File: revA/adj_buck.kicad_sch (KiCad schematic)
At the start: 31 parts, among them U26 LTC3600, U29 DAC121S101Q, U32 AD5270BRM

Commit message: exported init pdf
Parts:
- renumbered TP1 to TP3, TP2 to TP4
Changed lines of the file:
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@@
   (symbol (lib_id "Connector:TestPoint") (at 337.82 161.29 0) (unit 1)
     (in_bom yes) (on_board yes) (dnp no)
-    (property "Reference" "TP1" (at 340.36 157.353 0)
+    (property "Reference" "TP3" (at 340.36 157.353 0)
       (effects (font (size 1.27 1.27)) (justify left))
     )
@@
   (symbol (lib_id "Connector:TestPoint") (at 337.82 153.67 0) (unit 1)
     (in_bom yes) (on_board yes) (dnp no)
-    (property "Reference" "TP1" (at 340.36 149.733 0)
+    (property "Reference" "TP3" (at 340.36 149.733 0)
       (effects (font (size 1.27 1.27)) (justify left))
     )
@@
   (symbol (lib_id "Connector:TestPoint") (at 337.82 146.05 0) (unit 1)
     (in_bom yes) (on_board yes) (dnp no)
-    (property "Reference" "TP1" (at 340.36 142.113 0)
+    (property "Reference" "TP3" (at 340.36 142.113 0)
       (effects (font (size 1.27 1.27)) (justify left))
     )
@@
   (symbol (lib_id "Connector:TestPoint") (at 337.82 175.26 0) (unit 1)
     (in_bom yes) (on_board yes) (dnp no)
-    (property "Reference" "TP2" (at 340.36 171.323 0)
+    (property "Reference" "TP4" (at 340.36 171.323 0)
       (effects (font (size 1.27 1.27)) (justify left))
     )
@@
   (symbol (lib_id "Connector:TestPoint") (at 337.82 168.91 0) (unit 1)
     (in_bom yes) (on_board yes) (dnp no)
-    (property "Reference" "TP1" (at 340.36 164.973 0)
-      (effects (font (size 1.27 1.27)) (justify left))
-    )
+    (property "Reference" "TP3" (at 340.36 164.973 0)
+      (effects (font (size 1.27 1.27)) (justify left))
+    )

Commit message: working
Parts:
- added R95: 10k, Resistor_SMD:R_0603_1608Metric, symbol Device:R_US
- C44: renamed from C124; footprint (none) -> Capacitor_SMD:C_0805_2012Metric
- C45: renamed from C125; footprint (none) -> Capacitor_SMD:C_0603_1608Metric
- C46: renamed from C121; footprint (none) -> Capacitor_SMD:C_0805_2012Metric
- C47: renamed from C118; footprint (none) -> Capacitor_SMD:C_0603_1608Metric
- C48: renamed from C115; footprint (none) -> Capacitor_SMD:C_0805_2012Metric
- C49: renamed from C106; footprint (none) -> Capacitor_SMD:C_1206_3216Metric
- C50: renamed from C112; footprint (none) -> Capacitor_SMD:C_0603_1608Metric
- C51: renamed from C100; footprint (none) -> Capacitor_SMD:C_0805_2012Metric
- C52: renamed from C97; footprint (none) -> Capacitor_SMD:C_0603_1608Metric
- C53: renamed from C109; footprint (none) -> Capacitor_SMD:C_1206_3216Metric
- R54: renamed from R134; footprint (none) -> Resistor_SMD:R_0603_1608Metric
- R55: renamed from R15; footprint (none) -> Resistor_SMD:R_0603_1608Metric
- R56: renamed from R18; footprint (none) -> Resistor_SMD:R_0603_1608Metric
- R57: renamed from R110; footprint (none) -> Resistor_SMD:R_0603_1608Metric
- R58: renamed from R113; footprint (none) -> Resistor_SMD:R_0603_1608Metric
- R59: renamed from R137; footprint (none) -> Resistor_SMD:R_0603_1608Metric
- R93, R94, R95: footprint Resistor_SMD:R_0402_1005Metric -> Resistor_SMD:R_0603_1608Metric
- renumbered U29 to U14, U32 to U15, U26 to U16
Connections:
- net ~{SYNC}: now also R95.1
- new net +3V3: R95.2

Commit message: working
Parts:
- added R103: 0, Resistor_SMD:R_0603_1608Metric, symbol Device:R_US
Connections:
- net VSET: now also R103.1; no longer TP3.1
- new net: R103.2, TP3.1
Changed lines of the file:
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@@
+    (stroke (width 0) (type default))
+  )
+  (wire (pts (xy 327.66 146.05) (xy 337.82 146.05))
     (stroke (width 0) (type default))
   )
@@
     (stroke (width 0) (type default))
   )
-  (wire (pts (xy 325.12 146.05) (xy 337.82 146.05))
+  (wire (pts (xy 309.88 146.05) (xy 320.04 146.05))
     (stroke (width 0) (type default))
   )
@@
     (stroke (width 0) (type default))
   )
-  (rectangle (start 196.85 151.13) (end 248.92 180.34)
+  (rectangle (start 228.6 156.21) (end 280.67 185.42)
     (stroke (width 0) (type dash))
     (fill (type none))
@@
     (effects (font (size 5.08 5.08)) (justify left bottom))
   )
-  (text "OUTPUT VOLTAGE SETTING:" (at 198.12 154.94 0)
+  (text "OUTPUT VOLTAGE SETTING:" (at 229.87 160.02 0)
     (effects (font (size 1.905 1.905)) (justify left bottom))
   )
@@
   )
   (text "ISET pin voltage may be controlled \nby an external resistor, or an applied power\nsupply that has the capability to sink 50uA."
-    (at 198.12 162.56 0)
+    (at 229.87 167.64 0)
     (effects (font (size 1.27 1.27)) (justify left bottom))
   )
@@
   )
   (text "DAC121 (12b) or AD527(9b) control,\nDAC121 has rad data, can't simulate if \nit will work (no model) but probably will.\nAD527 doesn't have data but has been simulated."
-    (at 198.12 172.72 0)
+    (at 229.87 177.8 0)
     (effects (font (size 1.27 1.27)) (justify left bottom))
   )
@@
   )
   (text "No schedule for a re-spin, so \ncontrol methods are included."
-    (at 198.12 177.8 0)
+    (at 229.87 182.88 0)
     (effects (font (size 1.27 1.27)) (justify left bottom))
   )
@@
     (effects (font (size 1.27 1.27)) (justify left bottom))
   )
-  (label "VSET" (at 325.12 146.05 0) (fields_autoplaced)
+  (label "VSET" (at 309.88 146.05 0) (fields_autoplaced)
     (effects (font (size 1.27 1.27)) (justify left bottom))
   )
@@
         )
       )
+    )
+  )
+  (symbol (lib_id "Device:R_US") (at 323.85 146.05 90) (unit 1)
+    (in_bom yes) (on_board yes) (dnp no) (fields_autoplaced)
+    (property "Reference" "R103" (at 323.85 140.97 90)
+      (effects (font (size 1.27 1.27)))
+    )
+    (property "Value" "0" (at 323.85 143.51 90)
+      (effects (font (size 1.27 1.27)))
+    )
+    (property "Footprint" "Resistor_SMD:R_0603_1608Metric" (at 324.104 145.034 90)
+      (effects (font (size 1.27 1.27)) hide)
+    )
+    (property "Datasheet" "~" (at 323.85 146.05 0)
+      (effects (font (size 1.27 1.27)) hide)
+    )
+    (property "Manufacturer" "" (at 323.85 146.05 0)
+      (effects (font (size 1.27 1.27)) hide)
+    )
+    (property "Mfr. Part No" "" (at 323.85 146.05 0)
+      (effects (font (size 1.27 1.27)) hide)
+    )
+    (property "Description" "" (at 323.85 146.05 0)
+      (effects (font (size 1.27 1.27)) hide)
+    )
+    (pin "1")
+    (pin "2")
+    (instances
+      (project "magnetotorqer-drive-board"
+        (path "/612afcad-8da9-4dff-bf3c-8828929809ff/8ccdbec3-7661-4a0b-9858-5169c364aebb/5c5f6184-6b4f-4d2f-a4ab-4cc197c5e0c0"
+          (reference "R103") (unit 1)
+        )
+        (path "/612afcad-8da9-4dff-bf3c-8828929809ff/0c4bd054-86d6-4fc6-b8bd-5dc40d9d4357/5c5f6184-6b4f-4d2f-a4ab-4cc197c5e0c0"
+          (reference "R102") (unit 1)
+        )
+        (path "/612afcad-8da9-4dff-bf3c-8828929809ff/853a01c4-0f0d-42ee-a9e8-050403071668/5c5f6184-6b4f-4d2f-a4ab-4cc197c5e0c0"
+          (reference "R104") (unit 1)
+        )
+      )

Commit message: placement
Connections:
- net +3V3 renamed +3V3D
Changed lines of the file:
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@@
+      (effects (font (size 1.27 1.27)) hide)
+    )
+    (property "Manufacturer" "" (at 119.38 151.13 0)
+      (effects (font (size 1.27 1.27)) hide)
+    )
+    (property "Mfr. Part No" "" (at 119.38 151.13 0)
+      (effects (font (size 1.27 1.27)) hide)
+    )
+    (property "Description" "" (at 119.38 151.13 0)
       (effects (font (size 1.27 1.27)) hide)
     )

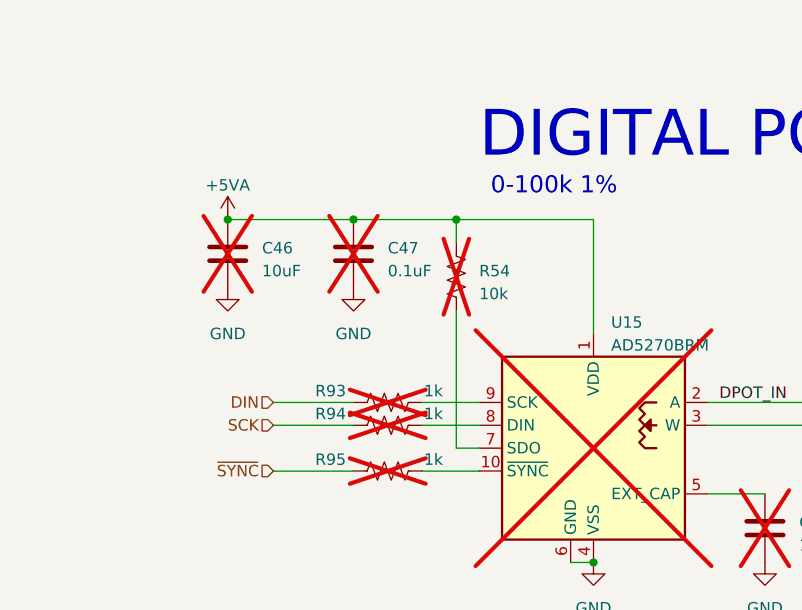
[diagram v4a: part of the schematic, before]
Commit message: routing mostly complete
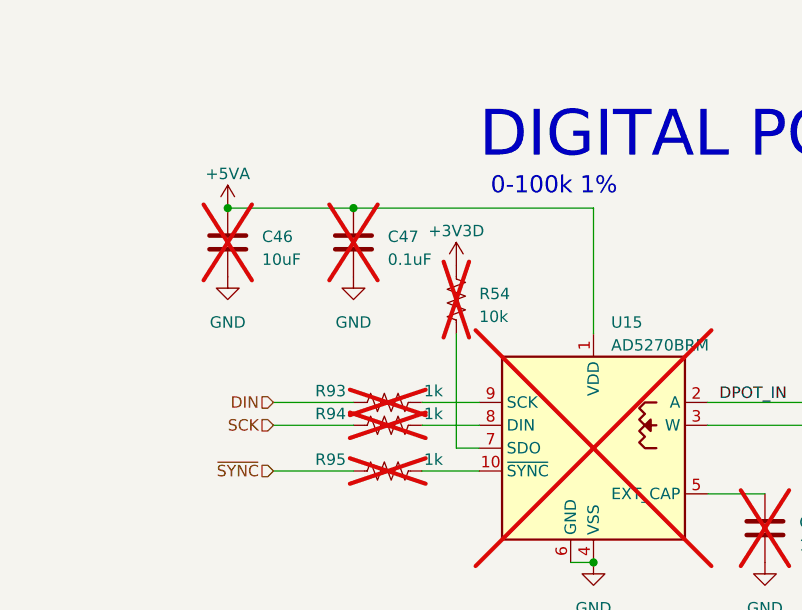
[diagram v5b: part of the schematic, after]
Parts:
- TP3, TP4: footprint TestPoint:TestPoint_Keystone_5000-5004_Miniature -> SierraLobo:TestPoint_Keystone_5000-5004_Miniature
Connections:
- net +3V3D: now also R54.1
- net +5VA: no longer R54.1
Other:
- moved on the sheet: C46, C47, R54

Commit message: working
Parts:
- TP3: Mfr. Part No 5119 -> 5000
- TP3: Mfr. Part No 5119 -> 5116
- TP3: Mfr. Part No 5119 -> 5004
- renumbered C49 to C44, C53 to C45, C52 to C46, C51 to C47, C44 to C48, C45 to C49, C46 to C51, C47 to C52, C48 to C53, R57 to R51, R59 to R52, R55 to R53, R58 to R55, R103 to R58, R54 to R60, R56 to R62, U16 to U14, U14 to U15, U15 to U16
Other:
- title: (none) -> SCHEMATIC, CUBESAT MAGNETORQER DRIVER

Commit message: worked review changes
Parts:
- C43: renamed from C48; Manufacturer (none) -> TDK Corporation; Mfr. Part No (none) -> CGA4J1X7S1E106K125AE; Value2 (none) -> 25V
- C44: renamed from C49; Manufacturer (none) -> TDK Corporation; Mfr. Part No (none) -> CGA3E2X7R1H104K080AE; Value2 (none) -> 50V
- C45: renamed from C51; Manufacturer (none) -> TDK Corporation; Mfr. Part No (none) -> CGA4J1X7S1E106K125AE; Value2 (none) -> 25V
- C46: renamed from C52; Manufacturer (none) -> TDK Corporation; Mfr. Part No (none) -> CGA3E2X7R1H104K080AE; Value2 (none) -> 50V
- C47: renamed from C53; Manufacturer (none) -> TDK Corporation; Mfr. Part No (none) -> CGA4J3X7R1H105K125AE; Value2 (none) -> 50V
- C48: renamed from C44; footprint Capacitor_SMD:C_1206_3216Metric -> Capacitor_SMD:C_1210_3225Metric; Manufacturer (none) -> TDK Corporation; Mfr. Part No (none) -> CGA6P1X7R1C226M250AC; Value2 (none) -> 16V
- C49: renamed from C50; Manufacturer (none) -> TDK Corporation; Mfr. Part No (none) -> CGA3E2C0G1H101J080AE; Value2 (none) -> 50V
- C50: renamed from C47; Manufacturer (none) -> TDK Corporation; Mfr. Part No (none) -> CGA4J3X7R1H105K125AE; Value2 (none) -> 50V
- C51: renamed from C46; Manufacturer (none) -> TDK Corporation; Mfr. Part No (none) -> CGA3E2X7R1H104K080AE; Value2 (none) -> 50V
- C52: renamed from C45; footprint Capacitor_SMD:C_1206_3216Metric -> Capacitor_SMD:C_1210_3225Metric; Manufacturer (none) -> TDK Corporation; Mfr. Part No (none) -> CGA6P1X7R1C226M250AC; Value2 (none) -> 16V
- L2: renamed from L3; footprint Inductor_SMD:L_Vishay_IHLP-2020 -> SierraLobo:L_Vishay_IHLP-2020
- R63: renamed from R60; Manufacturer (none) -> Stackpole Electronics Inc; Mfr. Part No (none) -> RMCF0603FT10K0; Value2 (none) -> 100mW
- R64: renamed from R53; Manufacturer (none) -> Stackpole Electronics Inc; Mfr. Part No (none) -> RMCF0603ZT0R00; Value2 (none) -> 100mW
- R65: renamed from R62; Manufacturer (none) -> Stackpole Electronics Inc; Mfr. Part No (none) -> RMCF0603ZT0R00; Value2 (none) -> 100mW
- R66: renamed from R51; Manufacturer (none) -> Stackpole Electronics Inc; Mfr. Part No (none) -> RMCF0603FT100K; Value2 (none) -> 100mW
- R67: renamed from R55; Manufacturer (none) -> Stackpole Electronics Inc; Mfr. Part No (none) -> RMCF0603FT100K; Value2 (none) -> 100mW
- R68: renamed from R52; Manufacturer (none) -> Stackpole Electronics Inc; Mfr. Part No (none) -> RMCF0603FT100K; Value2 (none) -> 100mW
- R69: renamed from R58; Manufacturer (none) -> Stackpole Electronics Inc; Mfr. Part No (none) -> RMCF0603ZT0R00; Value2 (none) -> 100mW
- R? (x2): renamed from R93; Manufacturer (none) -> Stackpole Electronics Inc; Mfr. Part No (none) -> RMCF0603FG1K00; Value2 (none) -> 100mW
- R? (x2): renamed from R95; Manufacturer (none) -> Stackpole Electronics Inc; Mfr. Part No (none) -> RMCF0603FG1K00; Value2 (none) -> 100mW
- R?: renamed from R95; Manufacturer (none) -> Stackpole Electronics Inc; Mfr. Part No (none) -> RMCF0603FT10K0; Value2 (none) -> 100mW
- R? (x2): renamed from R94; Manufacturer (none) -> Stackpole Electronics Inc; Mfr. Part No (none) -> RMCF0603FG1K00; Value2 (none) -> 100mW
- renumbered TP3 to TP?, TP4 to TP?, U15 to U13, U16 to U14, U14 to U15
